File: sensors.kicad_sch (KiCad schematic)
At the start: 18 parts, among them U4 ICM42605, U5 MMC5983MA, U6 ICP20100

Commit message: Finish R01B
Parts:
- removed U4: ICM42605, Package_LGA:LGA-14_3x2.5mm_P0.5mm_LayoutBorder3x4y, symbol ICM42605:ICM42605
- added C29: 0.1uF, Capacitor_SMD:C_0402_1005Metric, symbol Device:C
- added U4: ICM-20602, Package_LGA:LGA-16_3x3mm_P0.5mm_LayoutBorder3x5y, symbol Sensor_Motion:ICM-20602
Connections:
- net GND: now also C29.2, U4.10 (GND), U4.11 (GND), U4.12 (GND), U4.13 (GND), U4.15 (GND), U4.8 (FSYNC), U4.9 (GND)
- net PICO: now also U4.3 (SDA/SDI)
- net POCI: now also U4.4 (SAO/SD0)
- net SCK: now also U4.2 (SCL/SPC)
- net VDD: now also U4.1 (VDDIO), U4.16 (VDD)
- net nCS: now also U4.5 (~{CS})
- new net: C29.1, U4.14 (REGOUT)
- new net DRDY_ICM20602: U4.6 (INT)
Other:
- note added: "ICM-20602 IMU"
- note removed: "ICM-42605 IMU"
- moved on the sheet: C17, C18, C19, R7

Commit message: more work
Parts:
- added R23: 10K, Resistor_SMD:R_0402_1005Metric, symbol Device:R
- R7: DNP (none) -> [DNP]
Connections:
- net VDD: now also R23.1
- net nCS: now also R23.2
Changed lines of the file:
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@@
+    (stroke (width 0) (type default) (color 0 0 0 0))
+  )
+  (wire (pts (xy 19.05 72.39) (xy 19.05 74.93))
     (stroke (width 0) (type default) (color 0 0 0 0))
   )
@@
   )
   (wire (pts (xy 162.56 41.91) (xy 162.56 44.45))
+    (stroke (width 0) (type default) (color 0 0 0 0))
+  )
+  (wire (pts (xy 19.05 82.55) (xy 19.05 85.09))
     (stroke (width 0) (type default) (color 0 0 0 0))
   )
@@
     (effects (font (size 1.27 1.27)) (justify left))
   )
+  (hierarchical_label "VDD" (shape input) (at 19.05 72.39 90) (fields_autoplaced)
+    (effects (font (size 1.27 1.27)) (justify left))
+  )
   (hierarchical_label "SCL" (shape input) (at 148.59 52.07 180)
     (effects (font (size 1.27 1.27)) (justify right))
@@
   )
   (hierarchical_label "SCK" (shape input) (at 30.48 67.31 180)
+    (effects (font (size 1.27 1.27)) (justify right))
+  )
+  (hierarchical_label "nCS" (shape input) (at 19.05 85.09 270)
     (effects (font (size 1.27 1.27)) (justify right))
   )
@@
     (pin "2")
   )
+  (symbol (lib_id "Device:R") (at 19.05 78.74 0) (unit 1)
+    (in_bom yes) (on_board yes)
+    (property "Reference" "R23" (id 0) (at 21.59 77.4699 0)
+      (effects (font (size 1.27 1.27)) (justify left))
+    )
+    (property "Value" "10K" (id 1) (at 21.59 80.0099 0)
+      (effects (font (size 1.27 1.27)) (justify left))
+    )
+    (property "Footprint" "Resistor_SMD:R_0402_1005Metric" (id 2) (at 17.272 78.74 90)
+      (effects (font (size 1.27 1.27)) hide)
+    )
+    (property "Datasheet" "~" (id 3) (at 19.05 78.74 0)
+      (effects (font (size 1.27 1.27)) hide)
+    )
+    (property "LCSC" "C25744" (id 4) (at 19.05 78.74 0)
+      (effects (font (size 1.27 1.27)) hide)
+    )
+    (property "DNP" "[DNP]" (id 5) (at 24.13 82.55 0))
+    (pin "1")
+    (pin "2")
+  )
   (symbol (lib_id "power:GND") (at 60.96 64.77 90) (unit 1)
     (in_bom yes) (on_board yes) (fields_autoplaced)
@@
   )
   (symbol (lib_id "Device:R") (at 31.75 78.74 0) (unit 1)
-    (in_bom yes) (on_board yes) (fields_autoplaced)
+    (in_bom yes) (on_board yes)
     (property "Reference" "R7" (id 0) (at 34.29 77.4699 0)
       (effects (font (size 1.27 1.27)) (justify left))
@@
       (effects (font (size 1.27 1.27)) hide)
     )
+    (property "DNP" "[DNP]" (id 5) (at 36.83 82.55 0))
     (pin "1")
     (pin "2")

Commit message: R02B: finish new discussion modifications
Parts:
- removed C29: 0.1uF, Capacitor_SMD:C_0402_1005Metric, symbol Device:C
- removed R14, R15, R16, R17: 0, Resistor_SMD:R_0402_1005Metric, symbol Device:R
- removed U4: ICM-20602, Package_LGA:LGA-16_3x3mm_P0.5mm_LayoutBorder3x5y, symbol Sensor_Motion:ICM-20602
- added U4: ICM42605, Package_LGA:LGA-14_3x2.5mm_P0.5mm_LayoutBorder3x4y, symbol ICM42605:ICM42605
- C12: footprint Capacitor_SMD:C_0402_1005Metric -> Capacitor_SMD:C_0201_0603Metric
- C17: footprint Capacitor_SMD:C_0402_1005Metric -> Capacitor_SMD:C_0201_0603Metric; Mfr. # (none) -> CC0201MRX5R5BB225
- C18, C21, C22, C23: footprint Capacitor_SMD:C_0402_1005Metric -> Capacitor_SMD:C_0201_0603Metric; Mfr. # (none) -> CC0201KRX5R5BB104
- C19: footprint Capacitor_SMD:C_0402_1005Metric -> Capacitor_SMD:C_0201_0603Metric; Mfr. # (none) -> CC0201KRX5R5BB103
- R8, R9: footprint Resistor_SMD:R_0402_1005Metric -> Resistor_SMD:R_0201_0603Metric
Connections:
- net GND: now also U4.6 (GND), U4.9 (FSYNC)
- net PICO: now also U4.14 (SDA/SDI)
- net POCI: now also U4.1 (AD0/SDO)
- net SCK: now also U4.13 (SCL/SCLK)
- net VDD: now also U4.5 (VDDIO), U4.8 (VDD)
- net nCS: now also U4.12 (nCS)
- new net DRDY_ICM42605: U4.4 (INT)
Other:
- note added: "ICM-42605 IMU"
- note removed: "ICM-20602 IMU"
- moved on the sheet: C12, C17, C18, C19, C20, C21, R23, R7, R8, R9, U5

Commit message: h10: add graphics, fix drc, minor modifications
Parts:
- U4: footprint Package_LGA:LGA-14_3x2.5mm_P0.5mm_LayoutBorder3x4y -> ICM-42605:PQFN50P300X250X97-14N
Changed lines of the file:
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@@
       (effects (font (size 1.27 1.27)) (justify left))
     )
-    (property "Footprint" "Package_LGA:LGA-14_3x2.5mm_P0.5mm_LayoutBorder3x4y" (id 2) (at 29.21 33.02 0)
+    (property "Footprint" "ICM-42605:PQFN50P300X250X97-14N" (id 2) (at 29.21 33.02 0)
       (effects (font (size 1.27 1.27)) hide)
     )

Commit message: h10: r2 final
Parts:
- C12: LCSC C52923 -> (none)
- C17: LCSC C23733 -> (none); Mfr. # CC0201MRX5R5BB225 -> (none)
- C18, C21, C22, C23: LCSC C1525 -> (none); Mfr. # CC0201KRX5R5BB104 -> (none)
- C19: LCSC C15195 -> (none); Mfr. # CC0201KRX5R5BB103 -> (none)
- C20: LCSC C15525 -> (none)
- R23, R7: LCSC C25744 -> (none)
- R8, R9: LCSC C25867 -> (none)
- U5: LCSC C404329 -> (none)
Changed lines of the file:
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@@
       (effects (font (size 1.27 1.27)) hide)
     )
-    (property "LCSC" "C25867" (id 4) (at 67.31 85.09 0)
+    (property "LCSC" "" (id 4) (at 67.31 85.09 0)
       (effects (font (size 1.27 1.27)) hide)
     )
@@
       (effects (font (size 1.27 1.27)) hide)
     )
-    (property "LCSC" "C25744" (id 4) (at 19.05 85.09 0)
+    (property "LCSC" "" (id 4) (at 19.05 85.09 0)
       (effects (font (size 1.27 1.27)) hide)
     )
@@
       (effects (font (size 1.27 1.27)) hide)
     )
-    (property "LCSC" "C25744" (id 4) (at 27.94 85.09 0)
+    (property "LCSC" "" (id 4) (at 27.94 85.09 0)
       (effects (font (size 1.27 1.27)) hide)
     )
@@
       (effects (font (size 1.27 1.27)) hide)
     )
-    (property "LCSC" "C1525" (id 4) (at 176.53 44.45 0)
-      (effects (font (size 1.27 1.27)) hide)
-    )
-    (property "Mfr. #" "CC0201KRX5R5BB104" (id 5) (at 176.53 44.45 0)
+    (property "LCSC" "" (id 4) (at 176.53 44.45 0)
+      (effects (font (size 1.27 1.27)) hide)
+    )
+    (property "Mfr. #" "" (id 5) (at 176.53 44.45 0)
       (effects (font (size 1.27 1.27)) hide)
     )
@@
       (effects (font (size 1.27 1.27)) hide)
     )
-    (property "LCSC" "C1525" (id 4) (at 40.64 52.07 90)
-      (effects (font (size 1.27 1.27)) hide)
-    )
-    (property "Mfr. #" "CC0201KRX5R5BB104" (id 5) (at 40.64 52.07 0)
+    (property "LCSC" "" (id 4) (at 40.64 52.07 90)
+      (effects (font (size 1.27 1.27)) hide)
+    )
+    (property "Mfr. #" "" (id 5) (at 40.64 52.07 0)
       (effects (font (size 1.27 1.27)) hide)
     )
@@
       (effects (font (size 1.27 1.27)) hide)
     )
-    (property "LCSC" "C15195" (id 4) (at 60.96 52.07 0)
-      (effects (font (size 1.27 1.27)) hide)
-    )
-    (property "Mfr. #" "CC0201KRX5R5BB103" (id 5) (at 60.96 52.07 0)
+    (property "LCSC" "" (id 4) (at 60.96 52.07 0)
+      (effects (font (size 1.27 1.27)) hide)
+    )
+    (property "Mfr. #" "" (id 5) (at 60.96 52.07 0)
       (effects (font (size 1.27 1.27)) hide)
     )
@@
       (effects (font (size 1.27 1.27)) hide)
     )
-    (property "LCSC" "C23733" (id 4) (at 40.64 41.91 90)
-      (effects (font (size 1.27 1.27)) hide)
-    )
-    (property "Mfr. #" "CC0201MRX5R5BB225" (id 5) (at 40.64 41.91 0)
+    (property "LCSC" "" (id 4) (at 40.64 41.91 90)
+      (effects (font (size 1.27 1.27)) hide)
+    )
+    (property "Mfr. #" "" (id 5) (at 40.64 41.91 0)
       (effects (font (size 1.27 1.27)) hide)
     )
@@
       (effects (font (size 1.27 1.27)) hide)
     )
-    (property "LCSC" "C25867" (id 4) (at 76.2 85.09 0)
+    (property "LCSC" "" (id 4) (at 76.2 85.09 0)
       (effects (font (size 1.27 1.27)) hide)
     )
@@
       (effects (font (size 1.27 1.27)) hide)
     )
-    (property "LCSC" "C15525" (id 4) (at 123.19 64.77 0)
+    (property "LCSC" "" (id 4) (at 123.19 64.77 0)
       (effects (font (size 1.27 1.27)) hide)
     )
@@
       (effects (font (size 1.27 1.27)) hide)
     )
-    (property "LCSC" "C404329" (id 4) (at 110.49 55.88 0)
+    (property "LCSC" "" (id 4) (at 110.49 55.88 0)
       (effects (font (size 1.27 1.27)) hide)
     )
@@
       (effects (font (size 1.27 1.27)) hide)
     )
-    (property "LCSC" "C52923" (id 4) (at 100.33 44.45 90)
+    (property "LCSC" "" (id 4) (at 100.33 44.45 90)
       (effects (font (size 1.27 1.27)) hide)
     )
@@
       (effects (font (size 1.27 1.27)) hide)
     )
-    (property "LCSC" "C1525" (id 4) (at 120.65 44.45 0)
-      (effects (font (size 1.27 1.27)) hide)
-    )
-    (property "Mfr. #" "CC0201KRX5R5BB104" (id 5) (at 120.65 44.45 0)
+    (property "LCSC" "" (id 4) (at 120.65 44.45 0)
+      (effects (font (size 1.27 1.27)) hide)
+    )
+    (property "Mfr. #" "" (id 5) (at 120.65 44.45 0)
       (effects (font (size 1.27 1.27)) hide)
     )
@@
       (effects (font (size 1.27 1.27)) hide)
     )
-    (property "LCSC" "C1525" (id 4) (at 156.21 44.45 90)
-      (effects (font (size 1.27 1.27)) hide)
-    )
-    (property "Mfr. #" "CC0201KRX5R5BB104" (id 5) (at 156.21 44.45 0)
-      (effects (font (size 1.27 1.27)) hide)
-    )
+    (property "LCSC" "" (id 4) (at 156.21 44.45 90)
+      (effects (font (size 1.27 1.27)) hide)
+    )
+    (property "Mfr. #" "" (id 5) (at 156.21 44.45 0)
+      (effects (font (size 1.27 1.27)) hide)
+    )

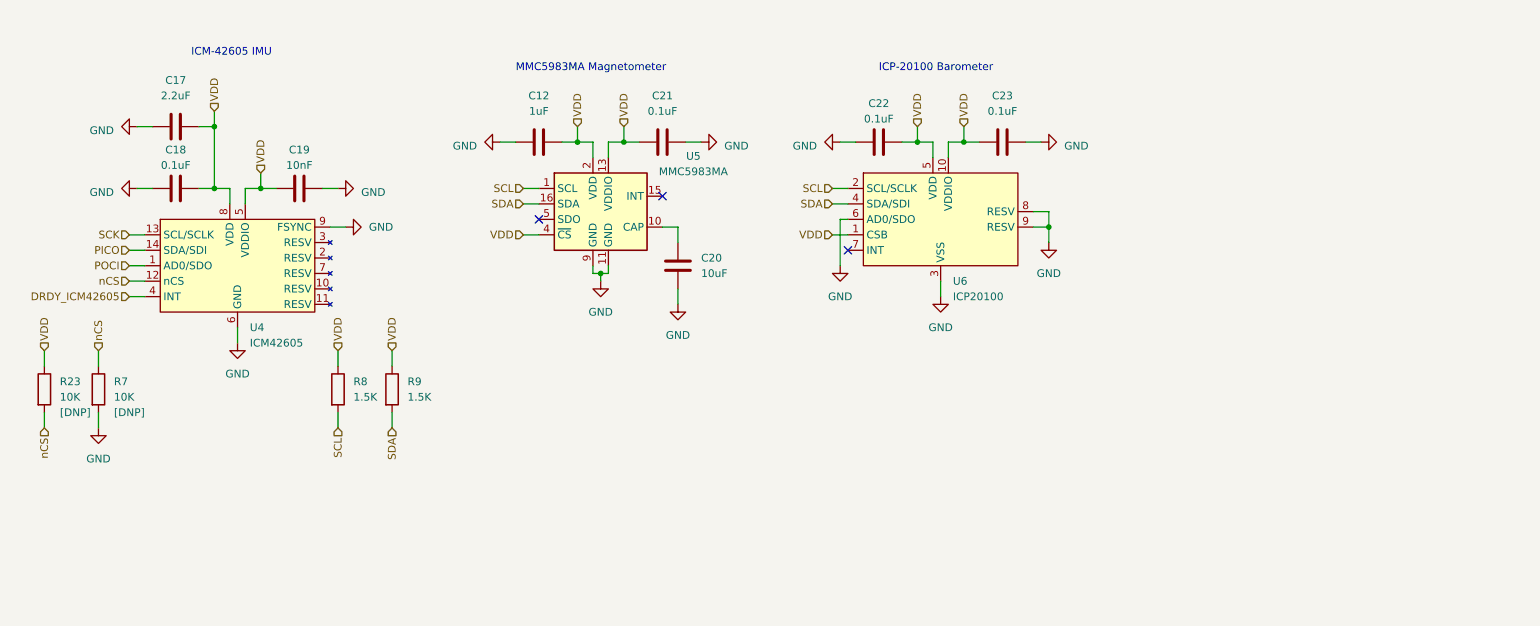
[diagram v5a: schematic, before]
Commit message: schematic: reformat and R3 release candidate
* reformat schematic
* minor fixes from R2 testing
* no functionality differences
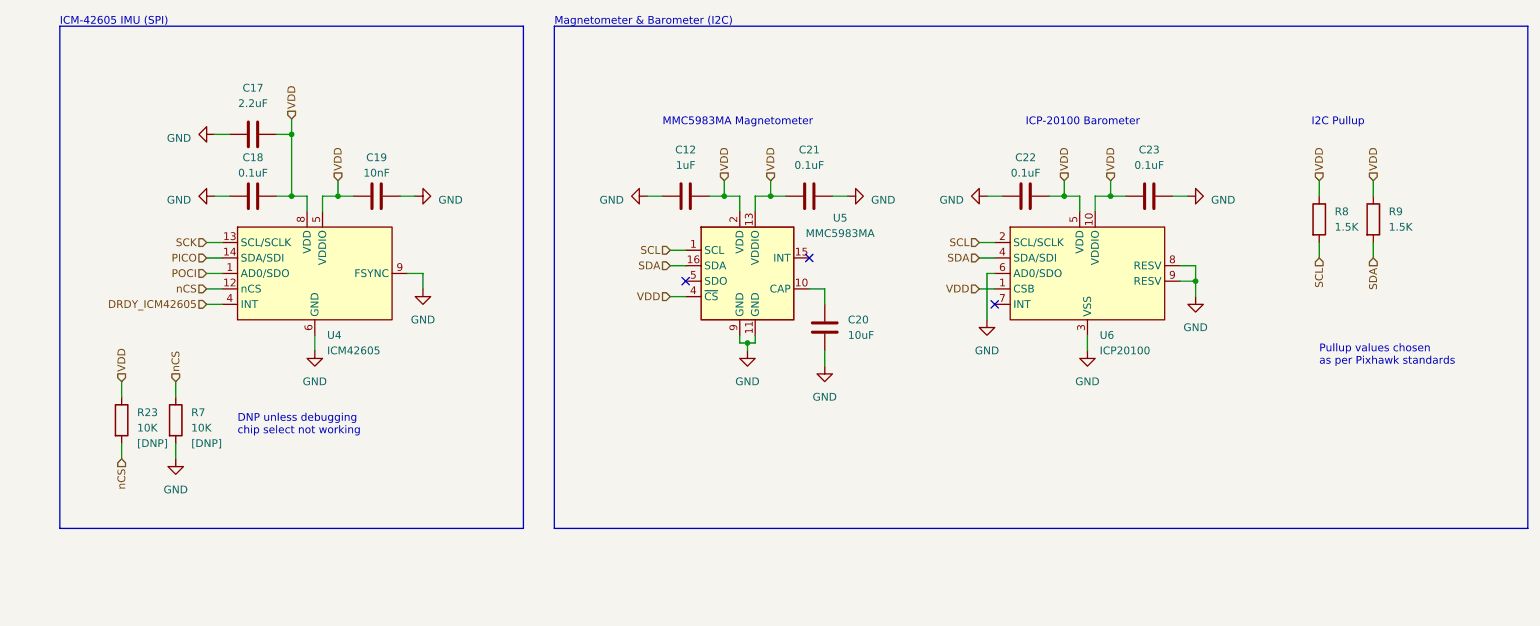
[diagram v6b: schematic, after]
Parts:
- U4: footprint ICM-42605:PQFN50P300X250X97-14N -> Package_LGA:LGA-14_3x2.5mm_P0.5mm_LayoutBorder3x4y
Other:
- note added: "DNP unless debugging chip select not working"
- note added: "I2C Pullup"
- note added: "ICM-42605 IMU (SPI)"
- note added: "Magnetometer & Barometer (I2C)"
- note added: "Pullup values chosen as per Pixhawk standards"
- note removed: "ICM-42605 IMU"
- company: (none) -> Kalyan S, Vincent W, Kai G, Kush N
- title: (none) -> Sensor Suite
- moved on the sheet: C12, C17, C18, C19, C20, C21, C22, C23, R23, R7, R8, R9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

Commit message: schematic: more improvements towards R3
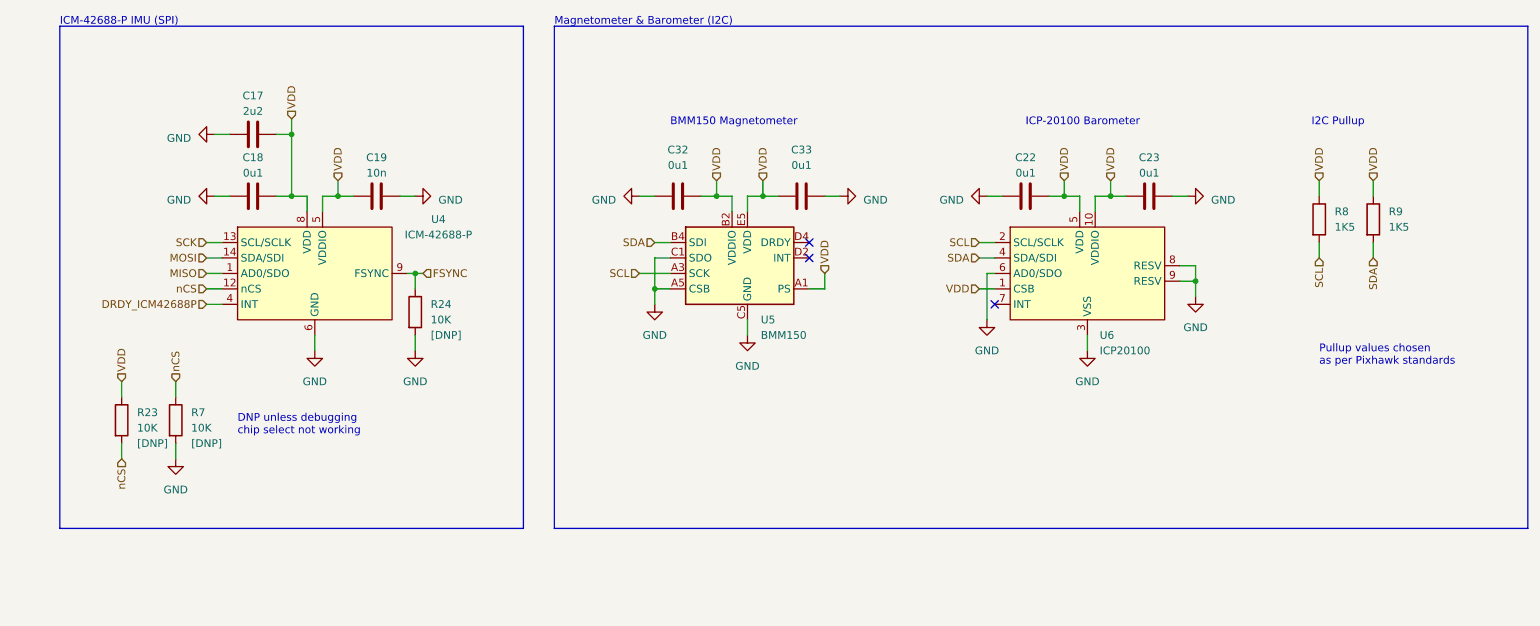
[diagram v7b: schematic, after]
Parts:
- removed C12: 1uF, Capacitor_SMD:C_0201_0603Metric, symbol Device:C
- removed C20: 10uF, Capacitor_SMD:C_0402_1005Metric, symbol Device:C
- removed C21: 0.1uF, Capacitor_SMD:C_0201_0603Metric, symbol Device:C
- removed U4: ICM42605, Package_LGA:LGA-14_3x2.5mm_P0.5mm_LayoutBorder3x4y, symbol ICM42605:ICM42605
- removed U5: MMC5983MA, Package_LGA:LGA-16_3x3mm_P0.5mm, symbol MMC5983MA:MMC5983MA
- added C32, C33: 0u1, Capacitor_SMD:C_0201_0603Metric, symbol Device:C
- added R24: 10K, Resistor_SMD:R_0201_0603Metric, symbol Device:R
- added U4: ICM-42688-P, Package_LGA:LGA-14_3x2.5mm_P0.5mm_LayoutBorder3x4y, symbol Sensor_Motion_Extra:ICM-42688-P
- added U5: BMM150, Package_CSP:WLCSP-12_1.56x1.56mm_P0.4mm, symbol Sensor_Magnetic:BMM150
- C17: value 2.2uF -> 2u2
- C18, C22, C23: value 0.1uF -> 0u1
- C19: value 10nF -> 10n
- R8, R9: value 1.5K -> 1K5
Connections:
- net GND: now also C32.1, C33.2, R24.2, U4.6 (GND), U5.A5 (CSB), U5.C1 (SDO), U5.C5 (GND), U5.E1 (GND), U5.E3 (GND)
- net SCK: now also U4.13 (SCL/SCLK)
- net SCL: now also U5.A3 (SCK)
- net SDA: now also U5.B4 (SDI)
- net VDD: now also C32.2, C33.1, U4.5 (VDDIO), U4.8 (VDD), U5.A1 (PS), U5.B2 (VDDIO), U5.E5 (VDD)
- net nCS: now also U4.12 (nCS)
- new net DRDY_ICM42688P: U4.4 (INT)
- new net FSYNC: R24.1, U4.9 (FSYNC)
- new net MISO: U4.1 (AD0/SDO)
- new net MOSI: U4.14 (SDA/SDI)
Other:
- note added: "BMM150 Magnetometer"
- note added: "ICM-42688-P IMU (SPI)"
- note removed: "ICM-42605 IMU (SPI)"
- note removed: "MMC5983MA Magnetometer"
- company: Kalyan S, Vincent W, Kai G, Kush N -> Kalyan S, Vincent W, Kai G

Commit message: schematic: refresh sensors, mcu and redo pinout
    * update rp2040 -> rp2350b
    * update icm-42688p -> icm-45686
    * update bmm150 -> bmm350
    * add current sensing logic
    * change pinout count and update pinout
    * drop led and heater support
    * add can termination
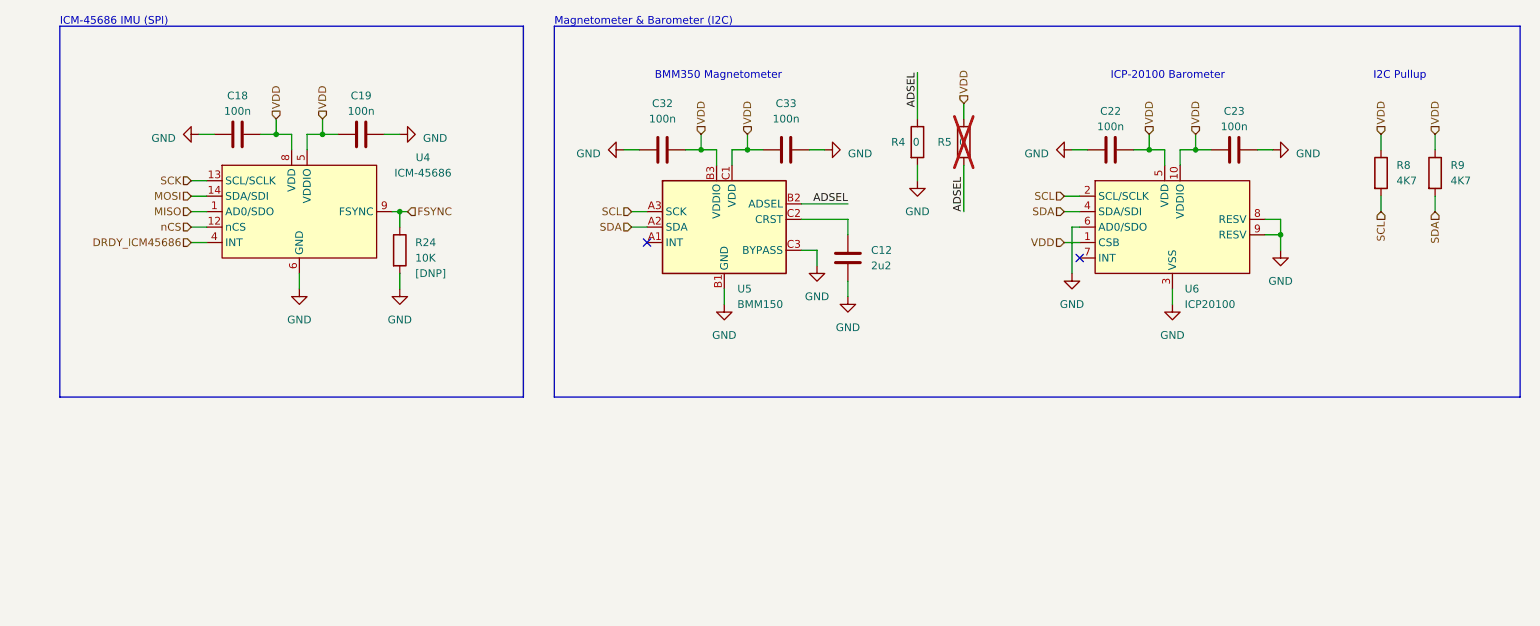
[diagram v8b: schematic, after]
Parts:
- removed C17: 2u2, Capacitor_SMD:C_0201_0603Metric, symbol Device:C
- removed R23, R7: 10K, Resistor_SMD:R_0402_1005Metric, symbol Device:R
- added C12: 2u2, symbol Device:C
- added R4, R5: 0, symbol Device:R
- C18, C22, C23, C32, C33: value 0u1 -> 100n
- C19: value 10n -> 100n
- R8, R9: value 1K5 -> 4K7
- U4: value ICM-42688-P -> ICM-45686; symbol Sensor_Motion_Extra:ICM-42688-P -> Sensor_Motion_Extra:ICM-45686
- U5: symbol Sensor_Magnetic:BMM150 -> Sensor_Magnetic_Extra:BMM350
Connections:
- net GND: now also U5.B1 (GND), U5.C3 (BYPASS), C12.1, R4.2; no longer U5.A5 (CSB), U5.C1 (SDO), U5.C5 (GND), U5.E1 (GND), U5.E3 (GND)
- net SDA: now also U5.A2 (SDA); no longer U5.B4 (SDI)
- net VDD: now also U5.B3 (VDDIO), U5.C1 (VDD), R5.2; no longer U5.A1 (PS), U5.B2 (VDDIO), U5.E5 (VDD)
- net DRDY_ICM42688P renamed DRDY_ICM45686
- new net: C12.2, U5.C2 (CRST)
- new net ADSEL: R4.1, R5.1, U5.B2 (ADSEL)
- no-connect marks 3 -> 2
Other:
- note added: "BMM350 Magnetometer"
- note added: "ICM-45686 IMU (SPI)"
- note removed: "BMM150 Magnetometer"
- note removed: "DNP unless debugging chip select not working"
- note removed: "ICM-42688-P IMU (SPI)"
- note removed: "Pullup values chosen as per Pixhawk standards"
- moved on the sheet: C18, C19, C22, C23, C32, C33, R24, R8, R9, U4, U6
